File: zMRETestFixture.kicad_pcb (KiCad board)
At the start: 2 copper layers, 129.5 x 127.6 mm, 209 parts, among them J1 Conn_01x01, J10 Conn_01x01, J11 Conn_01x01, J2 Conn_01x01, J3 Conn_01x01_Female, J4 Conn_01x01_Female, J5 Conn_01x01, J6 Conn_01x01, J7 Conn_01x01, J8 Conn_01x01, J9 Conn_02x05_Counter_Clockwise, SW1 SW_Push, SW2 SW_Push, U1 molex_48pin_MRE

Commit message: Updated https://github.com/rusefi/hw_microRusEfi/issues/163
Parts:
- removed R57: 5k, rusefi_lib:SM0805_jumper
- removed R59: 470k, rusefi_lib:SM0805_jumper
- added F1: 1A FUSE, rusefi_lib:Blank, F.Cu at (-19.7, 18.0)
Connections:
- SW1 pad 1: Net-(R57-Pad2) -> GND
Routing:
- net /5V2: track 136.9 -> 101.1 mm
- net Net-(R57-Pad2): track 12.9 -> 0.00 mm
- net GND: track 0.00 -> 5.75 mm

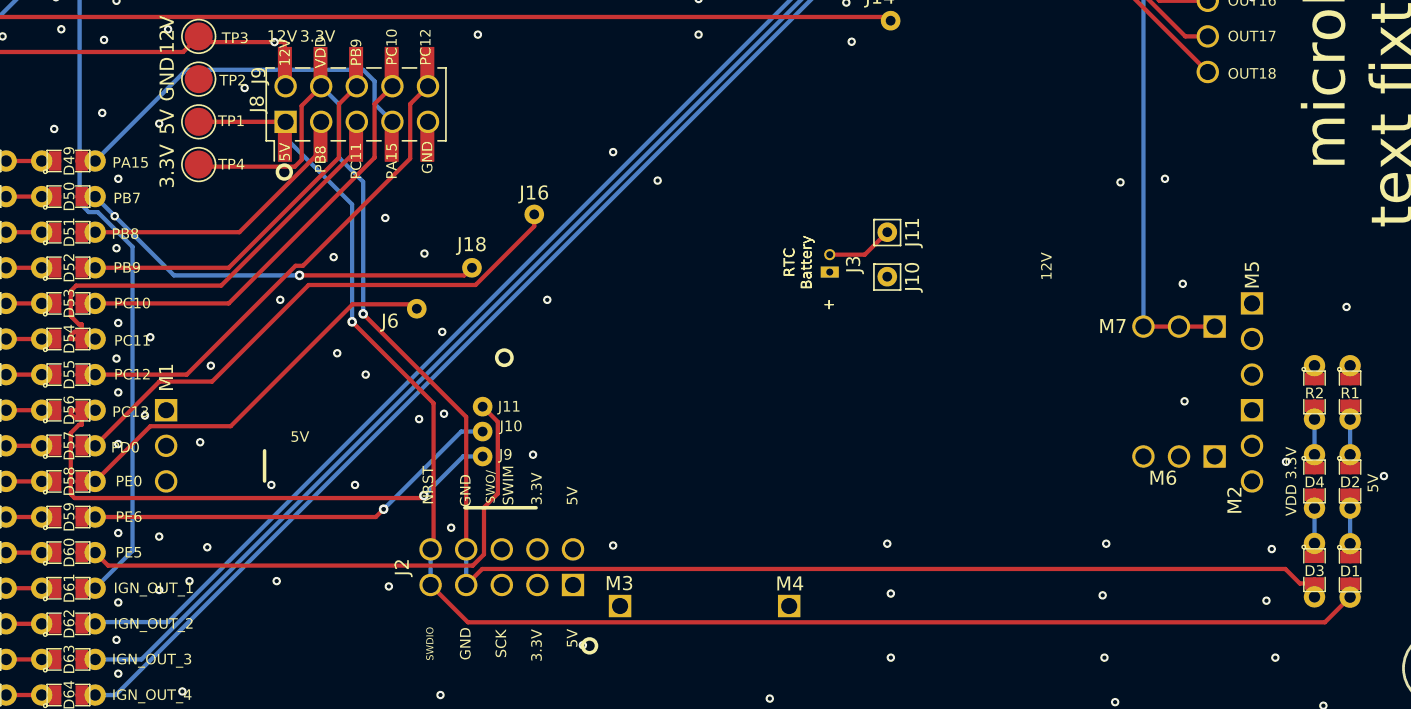
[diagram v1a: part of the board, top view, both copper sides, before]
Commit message: Fixed flipped J2 per https://github.com/rusefi/hw_microRusEfi/issues/179
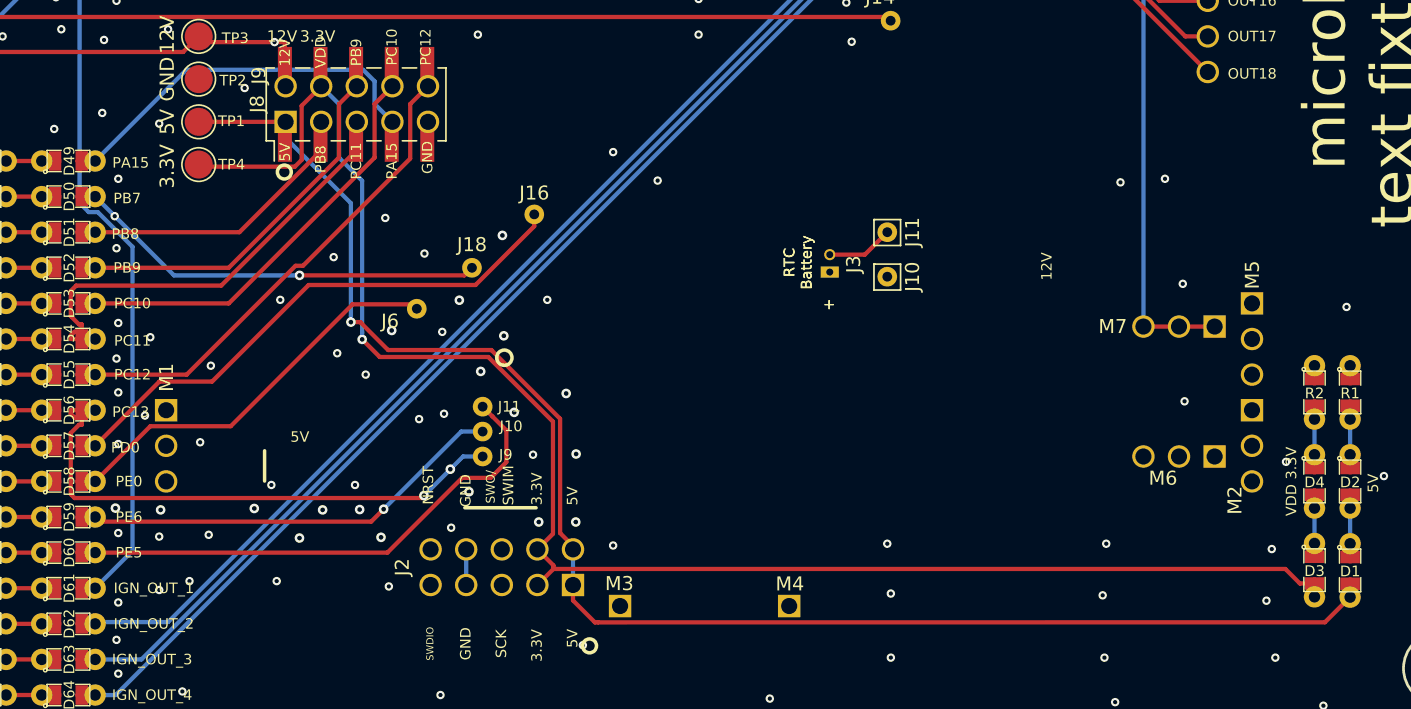
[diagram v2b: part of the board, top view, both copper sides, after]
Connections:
- U1 pad J201: (no net) -> /5V
- U1 pad J202: (no net) -> /5V
- U1 pad J203: GND -> /VDD
- U1 pad J204: GND -> /VDD
- U1 pad J207: /VDD -> GND
- U1 pad J208: /VDD -> GND
- U1 pad J209: /5V -> (no net)
- U1 pad J210: /5V -> (no net)
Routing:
- net /PE5: track 40.8 -> 37.6 mm
- net GND: track 5.75 -> 8.29 mm, vias 367 -> 385
- net /VDD: track 117.1 -> 118.9 mm
- net /5V: track 113.4 -> 112.6 mm
- net /PC13: vias 1 -> 2

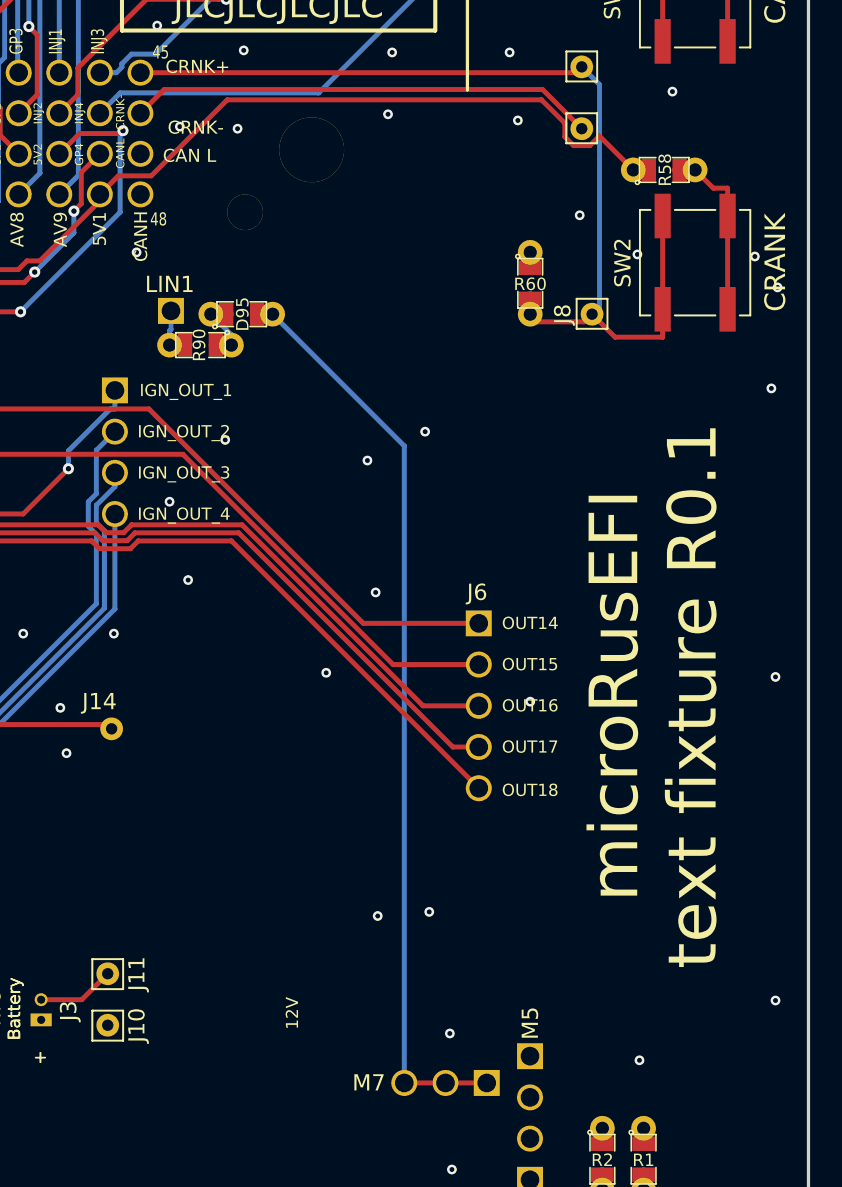
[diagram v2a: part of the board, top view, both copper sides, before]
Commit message: Bumped silk to to R0.2 and changed CRANK per https://github.com/rusefi/hw_microRusEfi/issues/177
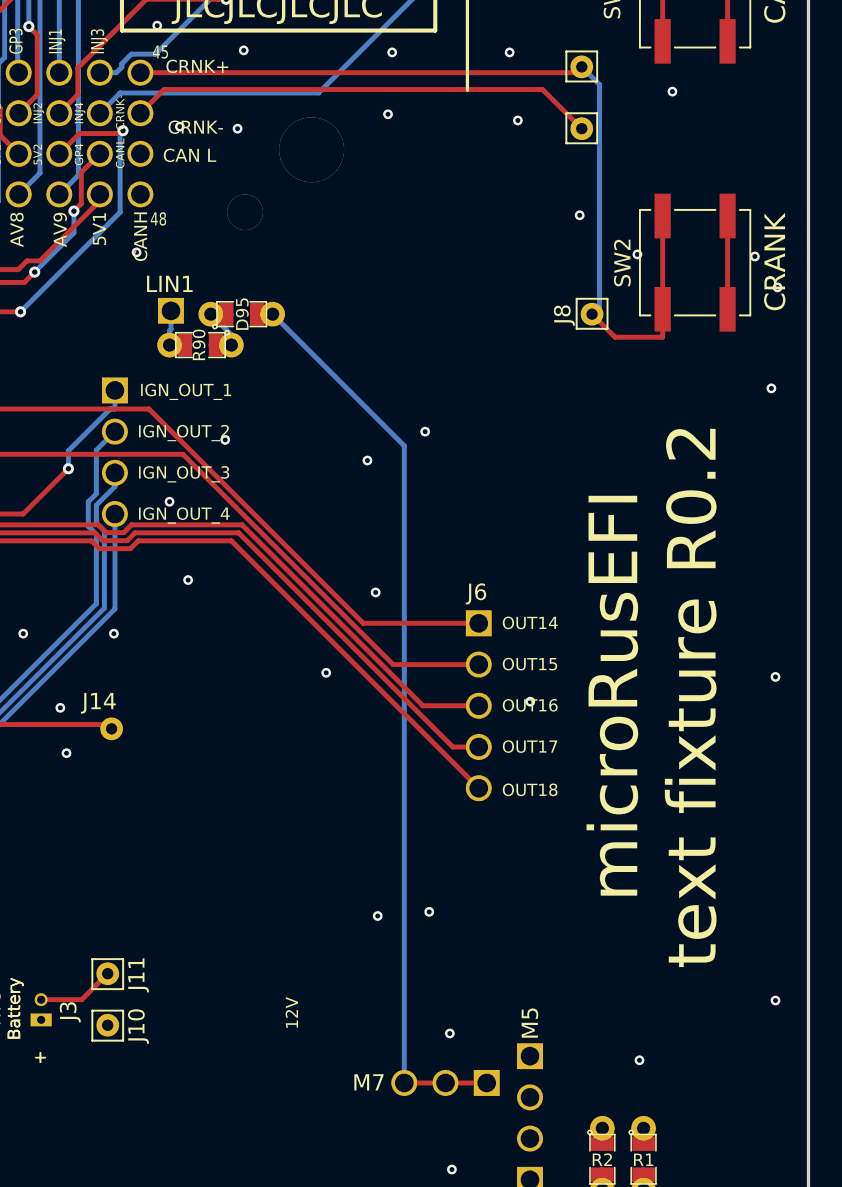
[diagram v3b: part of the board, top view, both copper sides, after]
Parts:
- removed R58: 5k, rusefi_lib:SM0805_jumper
- removed R60: 470k, rusefi_lib:SM0805_jumper
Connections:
- SW2 pad 1: Net-(R58-Pad2) -> GND
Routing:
- net /5V1: track 145.8 -> 106.7 mm
- net Net-(R58-Pad2): track 10.9 -> 0.00 mm
- net GND: track 8.29 -> 14.0 mm
- net /CRNK+: track 61.1 -> 55.6 mm
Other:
- board text added: "microRusEFI text fixture R0.2"
- board text removed: "microRusEFI text fixture R0.1"
